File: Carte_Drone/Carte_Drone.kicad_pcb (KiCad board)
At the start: 2 copper layers, 41.5 x 55 mm, 4 parts

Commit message: Modification typon
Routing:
- net Earth: track 31.2 -> 80.7 mm
- net /RXB: track 22.9 -> 34.5 mm
- net /RXG: track 16.6 -> 24.5 mm
- net /3V3: track 72.2 -> 79.0 mm
- net /TXB: track 24.2 -> 30.8 mm
- net /TXG: track 15.1 -> 17.3 mm
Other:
- board text added: "Projet Drone"
- board text removed: "Projet Drone Baptiste Rayan Bouna Abderrahmane"

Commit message: Changement empreinte 1
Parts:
- BLU1, GPS1: footprint Connector_PinSocket_1.27mm:PinSocket_1x06_P1.27mm_Vertical -> Librairie_Drone:PinSocket_1x06_P1.27mm_Vertical_2
- U3: footprint Connector_PinSocket_1.27mm:PinSocket_1x03_P1.27mm_Vertical -> Librairie_Drone:PinSocket_1x03_P1.27mm_Vertical_2
- moved BLU1 4.06 mm to (195.1, 89.3)
- moved GPS1 2.91 mm to (194.7, 72.6)

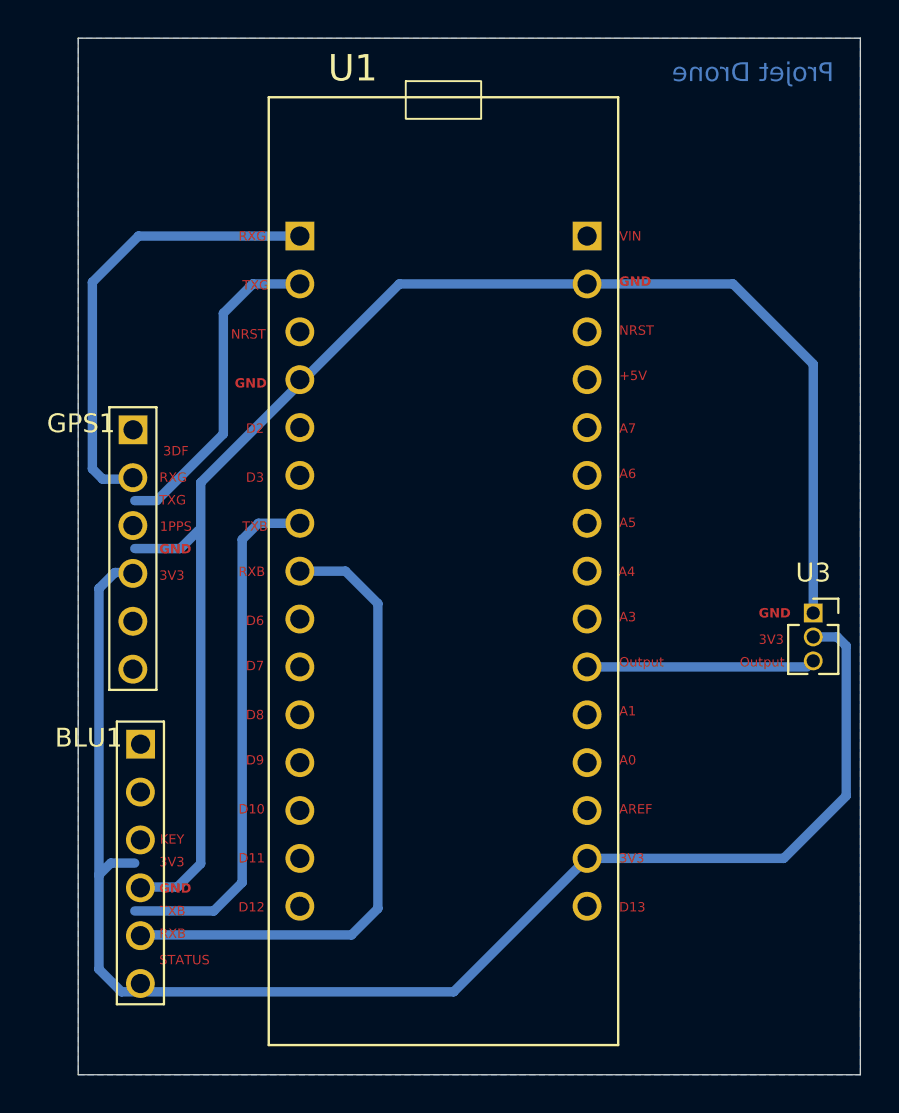
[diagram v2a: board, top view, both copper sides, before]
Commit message: Changement empreinte 2 et modification typon
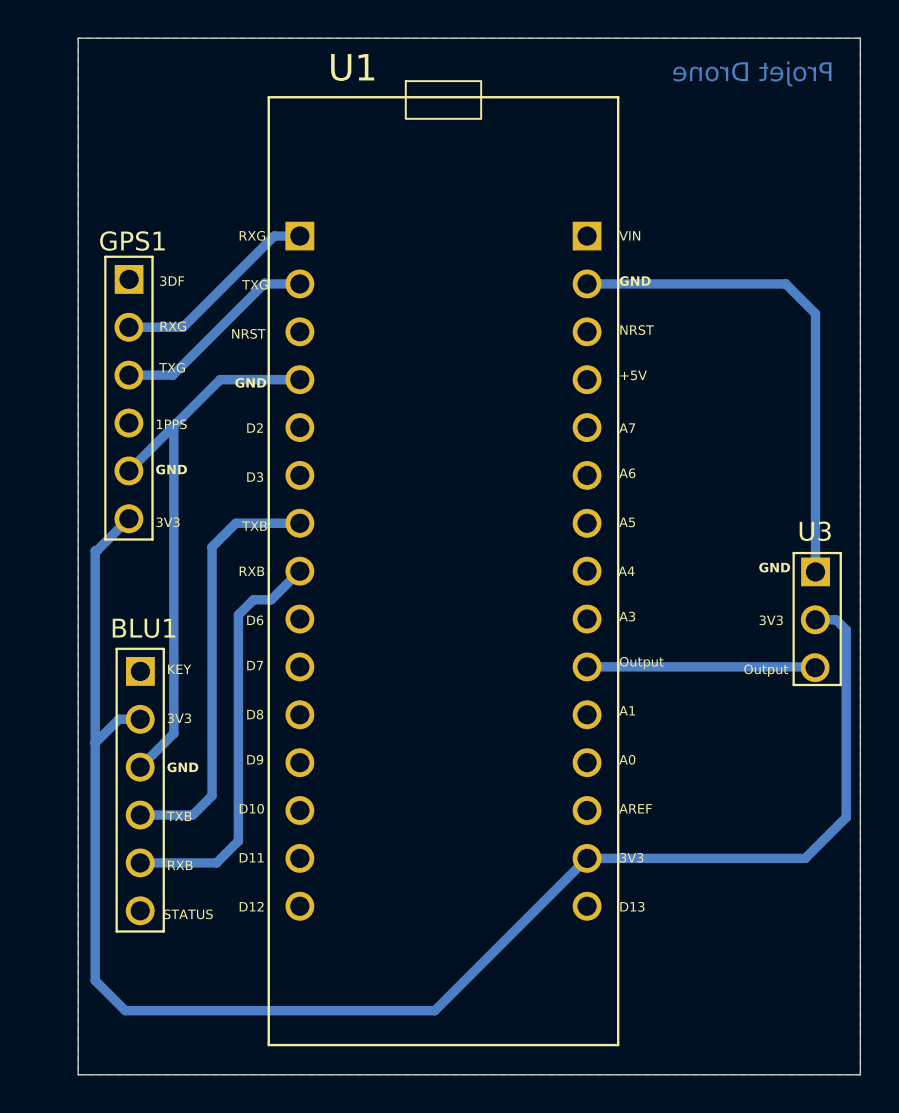
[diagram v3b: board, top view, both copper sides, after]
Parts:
- moved GPS1 7.98 mm to (194.4, 64.6)
- moved BLU1 3.86 mm to (195.0, 85.4)
- moved U3 3.35 mm to (231.0, 78.3)
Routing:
- net Earth: track 80.7 -> 56.4 mm
- net /RXG: track 24.5 -> 11.1 mm
- net /RXB: track 34.5 -> 21.9 mm
- net /TXB: track 30.8 -> 22.6 mm
- net /TXG: track 17.3 -> 11.1 mm
- net /3V3: track 79.0 -> 84.8 mm
